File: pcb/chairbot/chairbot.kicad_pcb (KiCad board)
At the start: 2 copper layers, 25 parts, among them J1 Conn_01x02, J2 Conn_01x05, J3 Conn_01x02, Q1 ZXMN4A06G, U1 ESP32mini, U2 74HCT08, U3 74HCT244, U4 buck-converter, U5 nRF24L01+, U6 Motor_driver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

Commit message: Work work work.
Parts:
- removed the REF** at (3.81, 96.0)
- removed the REF** at (49.5, 95.2)
- added C8: 100n, Capacitor_SMD:C_0603_1608Metric, F.Cu at (29.5, 59.4)
- added REF**: MountingHole_2.5mm, MountingHole:MountingHole_2.5mm, F.Cu at (3.68, 3.81)
- added REF**: MountingHole_2.5mm, MountingHole:MountingHole_2.5mm, F.Cu at (49.5, 94.9)
- added REF**: MountingHole_2.5mm, MountingHole:MountingHole_2.5mm, F.Cu at (3.56, 96.6)
- added REF**: MountingHole_2.5mm, MountingHole:MountingHole_2.5mm, F.Cu at (50.3, 4.32)
- added U8: AMS1117-3.3, Package_TO_SOT_SMD:SOT-223-3_TabPin2, F.Cu at (35.6, 57.9)
- moved C1 21.8 mm to (5.74, 34.4)
- moved C2 13.5 mm to (29.5, 56.2), turned to 270 degrees
- moved U3 11.3 mm to (5.59, 38.9)
- moved C4 9.86 mm to (44.2, 91.4)
- moved C3 9.31 mm to (24.9, 52.1)
- moved U2 6.45 mm to (11.4, 5.21)
- moved C5 1.44 mm to (11.6, 1.14)
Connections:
- C2 pad 2: +3V3 -> Net-(C2-Pad2)
- C3 pad 2: +3V3 -> Net-(C2-Pad2)
- J2 pad 1: (no net) -> +5V
- J2 pad 2: +3V3 -> (no net)
- U2 pad 12: (no net) -> +5V
- U2 pad 13: (no net) -> +5V
- U2 pad 4: (no net) -> GND
- U2 pad 5: Brake -> GND
- U2 pad 6: Net-(U2-Pad6) -> (no net)
- U5 pad 2: +3V3 -> Net-(C2-Pad2)
- U7 pad 3: Net-(U2-Pad6) -> Net-(U2-Pad3)
- U7 pad 4: Net-(U2-Pad6) -> Net-(U2-Pad3)
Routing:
- net GND: track 0.00 -> 129.7 mm, vias 0 -> 3
- net Net-(U2-Pad3): track 0.00 -> 72.4 mm
- net +5V: track 0.00 -> 62.5 mm
- net +24V: track 0.00 -> 62.3 mm, vias 0 -> 1
- net PWM_A_R: track 0.00 -> 32.3 mm
- net PWM_A_L: track 0.00 -> 32.0 mm
- net PWM_B_L: track 0.00 -> 26.7 mm
- net PWM_B_R: track 0.00 -> 24.4 mm
- net Net-(D2-Pad2): track 0.00 -> 21.4 mm, vias 0 -> 2
- net Net-(C2-Pad2): track 0.00 -> 21.4 mm
- net Net-(F1-Pad2): track 0.00 -> 10.0 mm
- net Brake: track 0.00 -> 8.92 mm, vias 0 -> 2
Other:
- board outline added: 54 x 100 mm

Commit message: Add remaining connections.
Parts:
- moved C3 88.6 mm to (61.5, 132.7)
- moved C4 88.6 mm to (80.8, 172.1)
- moved F1 88.6 mm to (39.9, 169.8)
- moved J3 88.6 mm to (74.9, 176.7)
- moved R1 88.6 mm to (45.5, 144.1)
- moved REF** 88.6 mm to (86.1, 175.5)
- moved U2 88.6 mm to (48.0, 85.9)
- moved U3 88.6 mm to (42.2, 119.5)
- moved U5 88.6 mm to (58.7, 134.2)
- moved U6 88.6 mm to (41.7, 90.8)
- moved U7 88.6 mm to (41.7, 144.1)
- moved C1 88.6 mm to (42.3, 115.1)
- moved C2 88.6 mm to (66.0, 136.8)
- moved C5 88.6 mm to (48.2, 81.8)
- moved C6 88.6 mm to (40.4, 101.2)
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
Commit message: Work on PCB.
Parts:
- added C10: 100n, Capacitor_SMD:C_0603_1608Metric, F.Cu at (77.3, 81.5)
- added C9: 10u, Capacitor_SMD:C_0805_2012Metric, F.Cu at (75.2, 106.7)
- added U9: PCA9515, Package_SO:TSSOP-8_3x3mm_P0.65mm, F.Cu at (77.3, 84.4)
- moved R1 39.4 mm to (63.6, 179.1)
- moved R2 23.1 mm to (63.6, 175.9)
- moved J3 4.81 mm to (79.6, 177.7)
- moved D2 4.45 mm to (69.7, 175.6)
- moved Q1 0.51 mm to (56.6, 175.1)
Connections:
- J2 pad 2: (no net) -> +3V3
- J2 pad 3: (no net) -> SDA1
- J2 pad 4: (no net) -> SCL1
- U1 pad 1: (no net) -> GND
- U1 pad 10: (no net) -> IO19
- U1 pad 12: (no net) -> IO23
- U1 pad 14: (no net) -> IO5
- U1 pad 16: (no net) -> +3V3
- U1 pad 22: (no net) -> GND
- U1 pad 25: (no net) -> SCL0
- U1 pad 26: (no net) -> Brake
- U1 pad 27: (no net) -> SDA0
- U1 pad 29: (no net) -> CE
- U1 pad 31: (no net) -> CS
- U1 pad 32: (no net) -> SCK
- U1 pad 33: (no net) -> GND
- U1 pad 34: (no net) -> MISO
- U1 pad 35: (no net) -> +5V
- U1 pad 36: (no net) -> MOSI
- U1 pad 7: (no net) -> EN
- U1 pad 8: (no net) -> IO18
- U2 pad 1: (no net) -> EN
- U2 pad 10: (no net) -> +5V
- U2 pad 9: (no net) -> +5V
- U3 pad 11: (no net) -> GND
- U3 pad 13: (no net) -> GND
- U3 pad 15: (no net) -> GND
- U3 pad 17: (no net) -> GND
- U3 pad 2: (no net) -> IO5
- U3 pad 4: (no net) -> IO18
- U3 pad 6: (no net) -> IO19
- U3 pad 8: (no net) -> IO23
- U5 pad 3: (no net) -> CE
- U5 pad 4: (no net) -> CS
- U5 pad 5: (no net) -> SCK
- U5 pad 6: (no net) -> MOSI
- U5 pad 7: (no net) -> MISO
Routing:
- net Brake: track 8.92 -> 147.8 mm, vias 2 -> 5
- net GND: track 129.7 -> 259.4 mm, vias 3 -> 5
- net +5V: track 62.5 -> 128.0 mm, vias 0 -> 2
- net MISO: track 0.00 -> 47.0 mm
- net MOSI: track 0.00 -> 41.5 mm
- net IO18: track 0.00 -> 28.8 mm, vias 0 -> 2
- net IO23: track 0.00 -> 28.7 mm, vias 0 -> 1
- net IO19: track 0.00 -> 27.7 mm, vias 0 -> 3
- net +3V3: track 0.00 -> 26.7 mm
- net SDA1: track 0.00 -> 21.7 mm
- net IO5: track 0.00 -> 20.8 mm, vias 0 -> 1
- net EN: track 0.00 -> 19.3 mm, vias 0 -> 2
- net SCL1: track 0.00 -> 18.7 mm
- net SDA0: track 0.00 -> 17.3 mm
- net SCL0: track 0.00 -> 14.0 mm
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
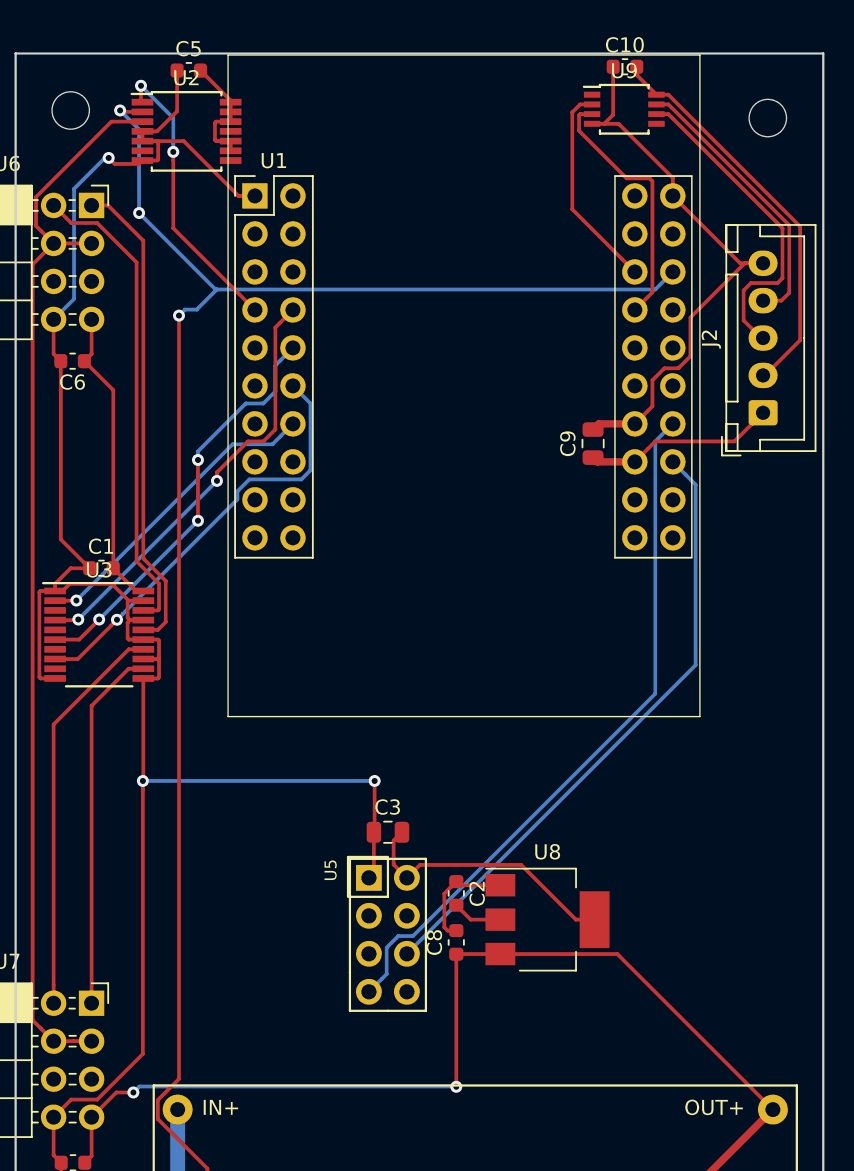
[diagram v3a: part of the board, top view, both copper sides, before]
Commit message: Finish routing.
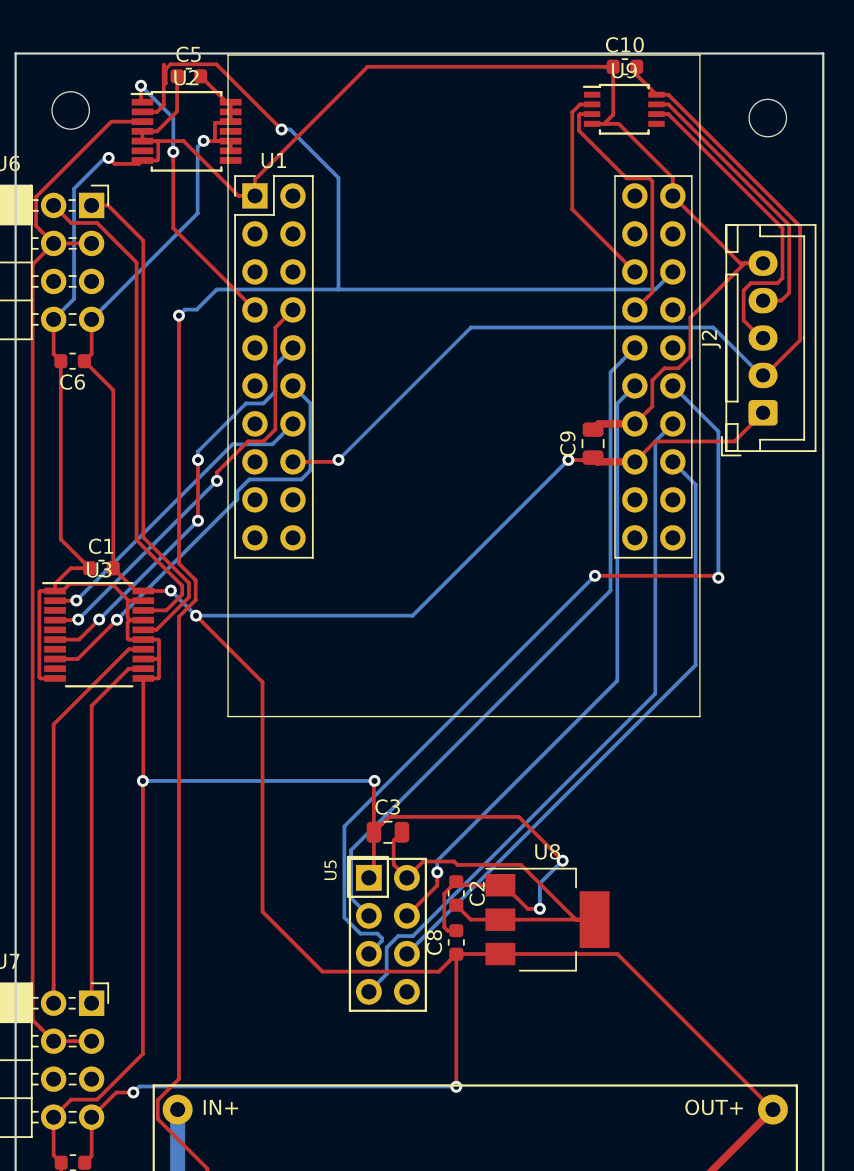
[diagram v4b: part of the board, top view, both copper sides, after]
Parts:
- moved C5 0.38 mm to (48.2, 82.2)
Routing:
- net +5V: track 128.0 -> 216.6 mm, vias 2 -> 6
- net SCK: track 0.00 -> 56.7 mm, vias 0 -> 2
- net GND: track 259.4 -> 308.6 mm, vias 5 -> 7
- net CE: track 0.00 -> 46.3 mm
- net CS: track 0.00 -> 41.7 mm, vias 0 -> 1
- net +3V3: track 26.7 -> 63.2 mm, vias 0 -> 1
- net Brake: track 147.8 -> 161.3 mm, vias 5 -> 4
- net Net-(C2-Pad2): track 21.4 -> 27.9 mm
- net PWM_A_L: track 32.0 -> 33.6 mm
- net PWM_A_R: track 32.3 -> 33.5 mm

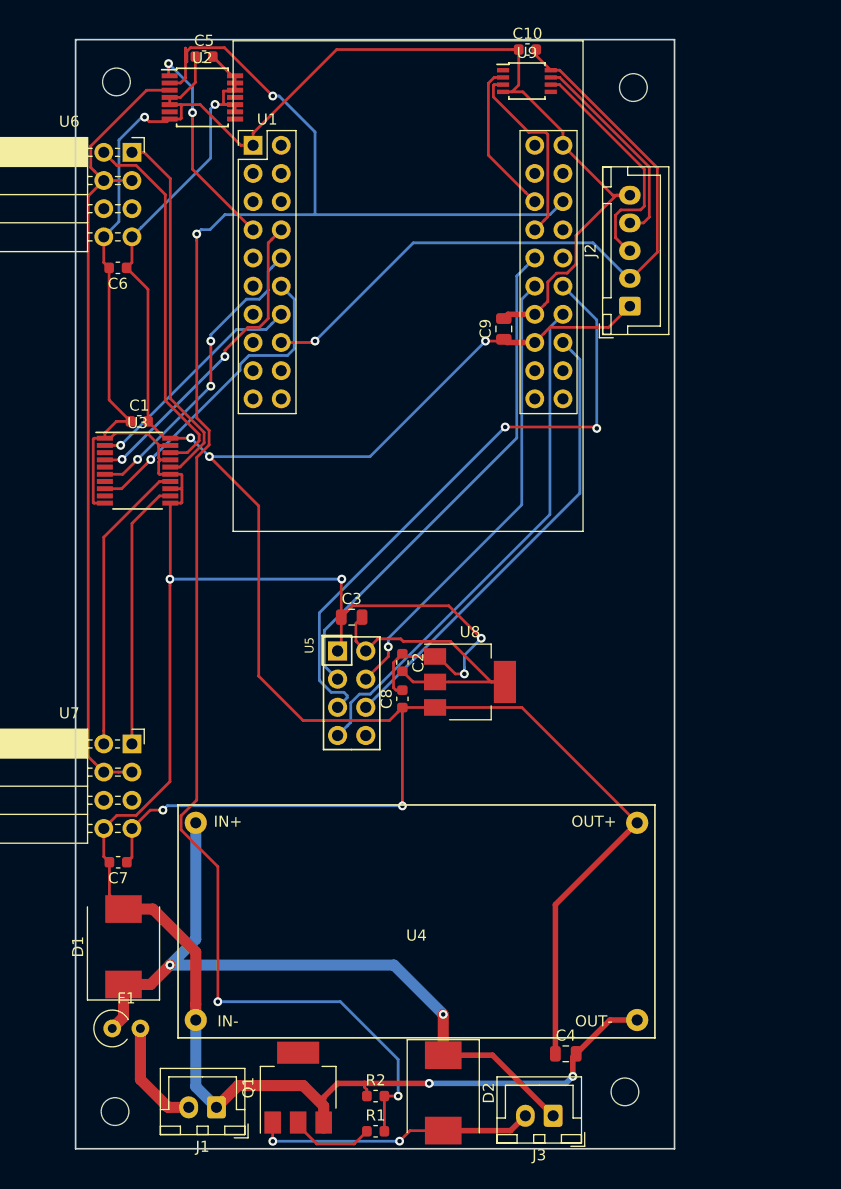
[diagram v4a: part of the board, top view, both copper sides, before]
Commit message: Add proper footprint for peak detector.
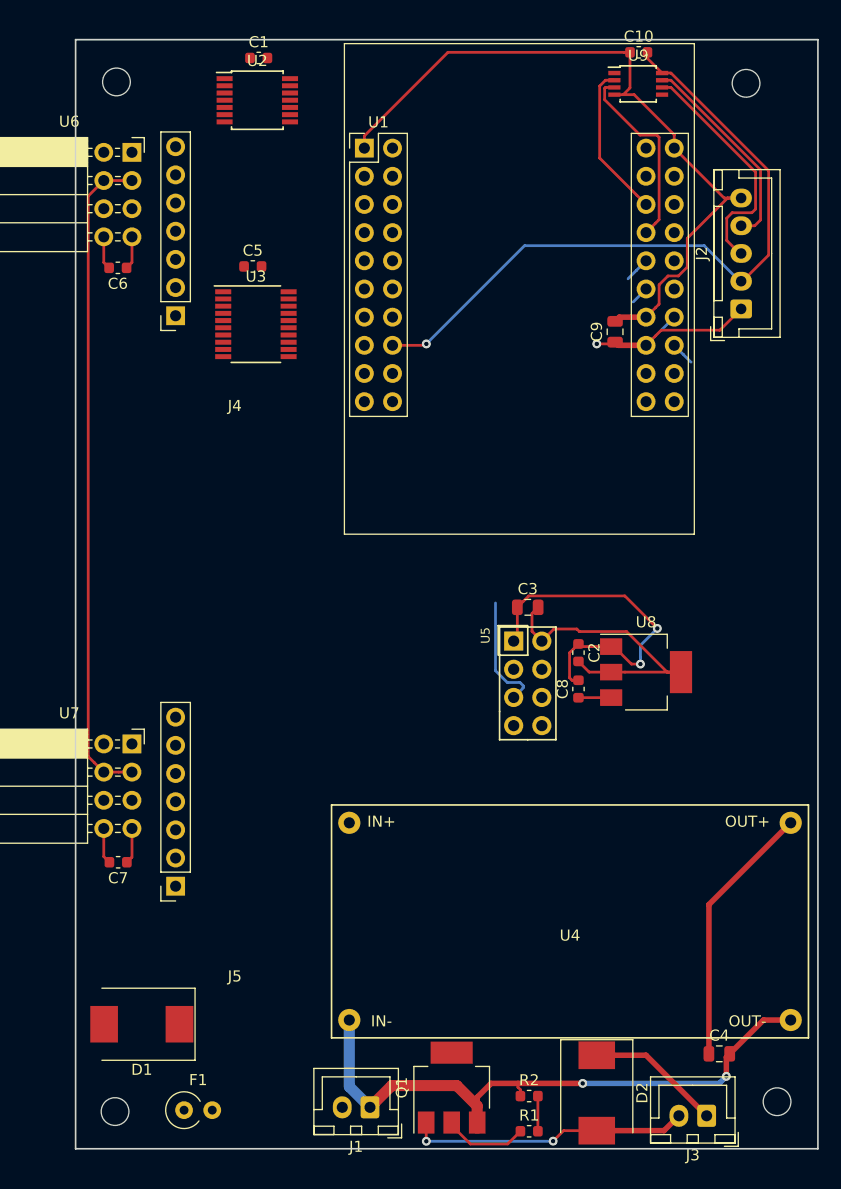
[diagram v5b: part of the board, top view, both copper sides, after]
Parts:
- added J4: Conn_01x07, chairbot:peakdetector, F.Cu at (45.6, 105.5)
- added J5: Conn_01x07, chairbot:peakdetector, F.Cu at (45.6, 157.0)
- moved C1 34.5 mm to (53.1, 82.3)
- moved C5 19.4 mm to (52.6, 101.1)
- moved U3 17.0 mm to (52.8, 106.3)
- moved U5 15.9 mm to (74.5, 133.3)
- moved C2 15.9 mm to (81.9, 135.9)
- moved C3 15.9 mm to (77.3, 131.8)
- moved C8 15.9 mm to (81.9, 139.2)
- moved U8 15.9 mm to (88.0, 137.7)
- moved D2 13.8 mm to (83.6, 175.6)
- moved U4 13.8 mm to (81.2, 160.1)
- moved J1 13.8 mm to (63.1, 176.9)
- moved Q1 13.8 mm to (70.5, 175.1)
- moved R1 13.8 mm to (77.5, 179.1)
- moved R2 13.8 mm to (77.5, 175.9)
- moved C4 13.8 mm to (94.6, 172.1)
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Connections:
- U6 pad 5: (no net) -> IS_A_R
- U6 pad 6: (no net) -> IS_A_L
- U7 pad 5: (no net) -> IS_B_R
- U7 pad 6: (no net) -> IS_B_L
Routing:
- net +5V: track 216.6 -> 47.6 mm, vias 6 -> 1
- net Brake: track 161.3 -> 3.17 mm, vias 4 -> 0
- net GND: track 308.6 -> 163.0 mm, vias 7 -> 4
- net +24V: track 65.4 -> 12.2 mm, vias 2 -> 0
- net SCK: track 56.7 -> 10.6 mm, vias 2 -> 0
- net MISO: track 47.0 -> 1.66 mm
- net CE: track 46.3 -> 2.30 mm
- net CS: track 41.7 -> 1.66 mm, vias 1 -> 0
- net MOSI: track 41.5 -> 2.16 mm
- net PWM_A_L: track 33.6 -> 0.00 mm
- net PWM_A_R: track 33.5 -> 0.00 mm
- net IO18: track 28.8 -> 0.00 mm, vias 2 -> 0
- net IO23: track 28.7 -> 0.00 mm, vias 1 -> 0
- net IO19: track 27.7 -> 0.00 mm, vias 3 -> 0
- net PWM_B_L: track 26.7 -> 0.00 mm
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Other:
- board size 54 x 100 mm -> 66.9 x 100 mm

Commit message: Do more routing.
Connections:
- J4 pad 3: (no net) -> IS_A_L_P
- J4 pad 5: (no net) -> IS_A_R_P
- J5 pad 3: (no net) -> IS_B_L_P
- J5 pad 5: (no net) -> IS_B_R_P
- U1 pad 11: (no net) -> IS_B_L_P
- U1 pad 28: (no net) -> IS_A_R_P
- U1 pad 6: (no net) -> IS_A_L_P
- U1 pad 9: (no net) -> IS_B_R_P
- U3 pad 16: PWM_A_R -> PWM_A_L
- U3 pad 18: PWM_A_L -> PWM_A_R
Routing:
- net GND: track 163.0 -> 298.7 mm, vias 4 -> 5
- net +5V: track 47.6 -> 135.9 mm, vias 1 -> 3
- net +24V: track 12.2 -> 76.9 mm
- net IS_A_R_P: track 0.00 -> 46.1 mm
- net Brake: track 3.17 -> 48.9 mm, vias 0 -> 1
- net PWM_A_R: track 0.00 -> 35.7 mm, vias 0 -> 1
- net PWM_A_L: track 0.00 -> 30.6 mm, vias 0 -> 2
- net IS_A_L_P: track 0.00 -> 24.9 mm, vias 0 -> 1
- net IO19: track 0.00 -> 22.9 mm, vias 0 -> 1
- net EN: track 0.00 -> 20.6 mm
- net IO18: track 0.00 -> 18.3 mm, vias 0 -> 1
- net IO23: track 0.00 -> 17.3 mm, vias 0 -> 2
- net IO5: track 0.00 -> 16.0 mm, vias 0 -> 1
- net Net-(U2-Pad3): track 59.6 -> 72.1 mm, vias 0 -> 1
- net Net-(F1-Pad2): track 0.00 -> 11.8 mm
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
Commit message: Finalize layout.
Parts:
- moved REF** 3.00 mm to (100.0, 85.0)
- moved REF** 0.62 mm to (100.0, 177.0)
- moved REF** 0.60 mm to (40.0, 85.0)
- moved REF** 0.32 mm to (40.0, 177.0)
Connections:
- U3 pad 12: PWM_B_R -> PWM_B_L
- U3 pad 14: PWM_B_L -> PWM_B_R
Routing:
- net +5V: track 135.9 -> 250.2 mm
- net Brake: track 48.9 -> 148.3 mm, vias 1 -> 2
- net IS_B_L_P: track 0.00 -> 67.1 mm, vias 0 -> 1
- net IS_B_R_P: track 0.00 -> 62.9 mm, vias 0 -> 1
- net GND: track 298.7 -> 360.1 mm, vias 5 -> 8
- net MISO: track 0.00 -> 51.3 mm
- net CE: track 0.00 -> 48.4 mm, vias 0 -> 1
- net PWM_B_R: track 0.00 -> 44.9 mm
- net PWM_B_L: track 0.00 -> 43.9 mm
- net CS: track 0.00 -> 42.8 mm, vias 0 -> 1
- net SCK: track 10.6 -> 53.3 mm, vias 0 -> 1
- net MOSI: track 0.00 -> 42.2 mm
- net IO19: track 22.9 -> 26.2 mm

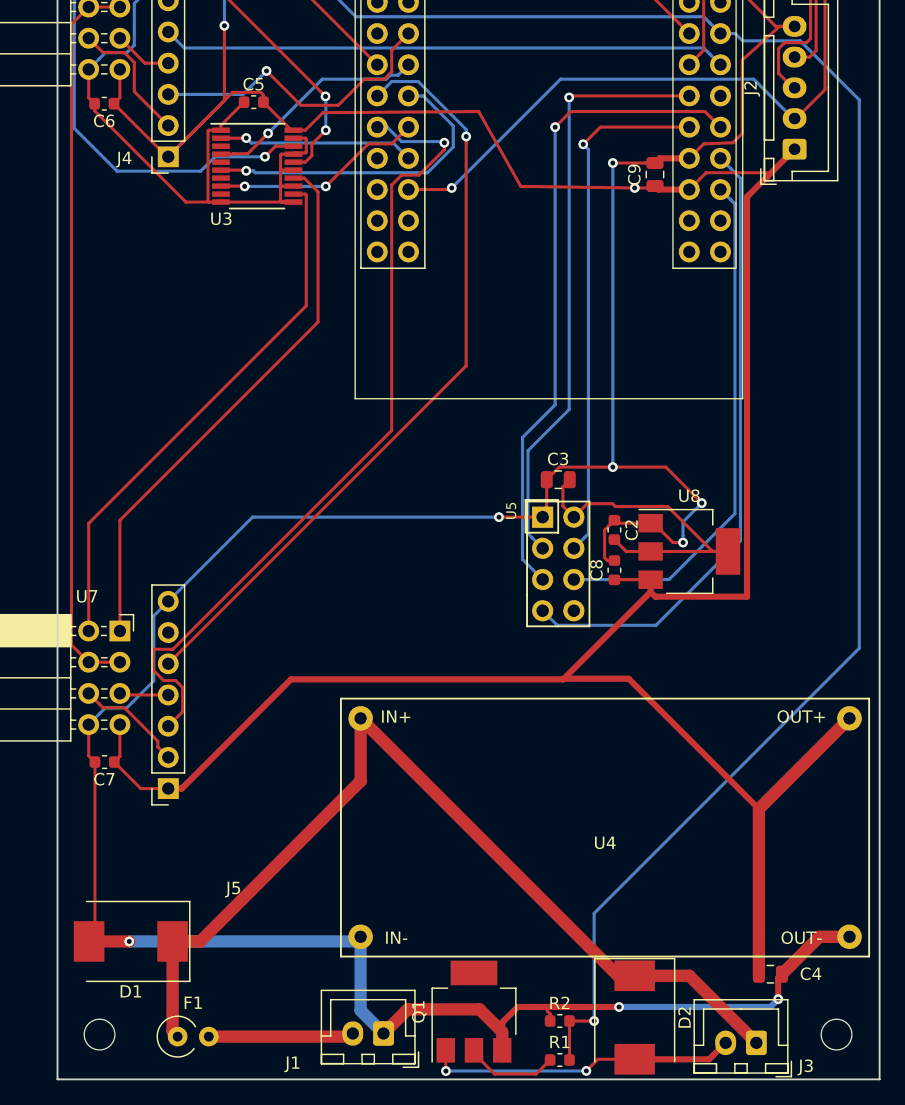
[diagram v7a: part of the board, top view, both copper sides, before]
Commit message: Fix footprint for diodes.
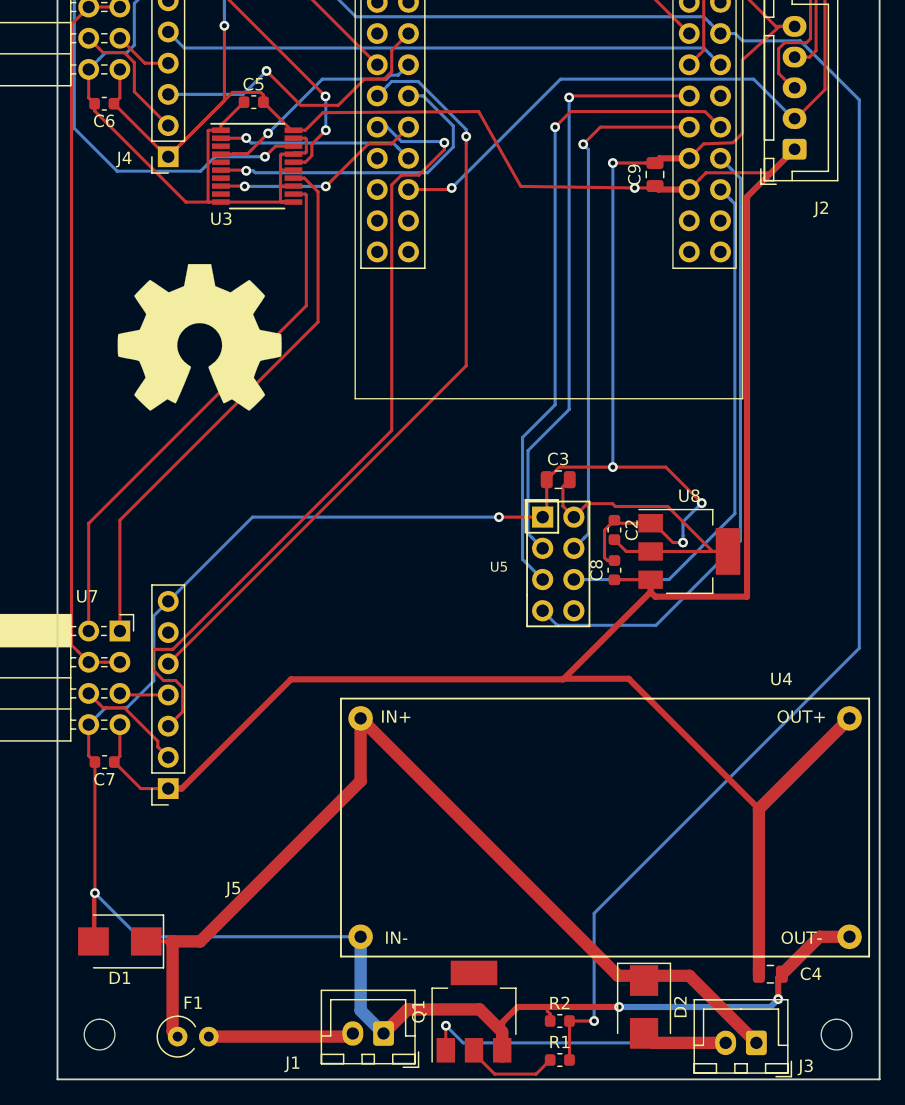
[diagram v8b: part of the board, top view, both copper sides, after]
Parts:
- added REF**: OSHW-Symbol_13.4x12mm_SilkScreen, Symbol:OSHW-Symbol_13.4x12mm_SilkScreen, F.Cu at (48.1, 120.3)
- D1, D2: footprint Diode_SMD:D_SMC -> Diode_SMD:D_SMB
- moved D2 1.15 mm to (84.3, 174.8)
- moved D1 0.89 mm to (41.7, 169.4)
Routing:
- net Net-(D2-Pad2): track 25.4 -> 32.3 mm, vias 2 -> 1
- net GND: track 360.1 -> 364.2 mm
- net +24V: track 76.9 -> 79.5 mm
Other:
- rule pad_to_mask_clearance: 0.2 -> -0.2
- board text added: "https://github.com/bullestock/chairbot/"
